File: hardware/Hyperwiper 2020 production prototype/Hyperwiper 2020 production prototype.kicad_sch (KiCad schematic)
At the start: 19 parts, among them K1 Main Power relay, K2 Wiper control relay, Q1 PN2222A, SW1 ON-OFF, U1 Teensy4.0, U3 L7805

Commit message: Updated Schematic and board.
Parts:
- added X1, X2: W237-3E-bGeigieNanoKit_V1.1r5a-eagle-import, DWP 2020:W237-3E, symbol import_from_eagle-rescue:W237-3E-bGeigieNanoKit_V1.1r5a-eagle-import
- RV1: footprint Potentiometer_THT:Potentiometer_Alps_RK09K_Single_Horizontal -> Potentiometer_THT:Potentiometer_Piher_PT-10-V05_Vertical
- U3: footprint Package_TO_SOT_THT:TO-220-3_Vertical -> Package_TO_SOT_THT:TO-220-3_Horizontal_TabUp
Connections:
- net GND: now also X1.1 (KL)
- net reed: now also X1.2 (KL)
- net at K1.1, K2.3: now also X2.1 (KL)
- net at K1.4, K1.5, K2.1: now also X2.2 (KL)
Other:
- moved on the sheet: S1
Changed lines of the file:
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@@
+    (stroke (width 0) (type solid) (color 0 0 0 0))
+  )
+  (wire (pts (xy 234.95 114.3) (xy 252.73 114.3))
+    (stroke (width 0) (type solid) (color 0 0 0 0))
+  )
+  (wire (pts (xy 234.95 116.84) (xy 242.57 116.84))
+    (stroke (width 0) (type solid) (color 0 0 0 0))
+  )
+  (wire (pts (xy 234.95 118.11) (xy 234.95 116.84))
     (stroke (width 0) (type solid) (color 0 0 0 0))
   )
@@
     (stroke (width 0) (type solid) (color 0 0 0 0))
   )
+  (wire (pts (xy 242.57 116.84) (xy 242.57 118.11))
+    (stroke (width 0) (type solid) (color 0 0 0 0))
+  )
+  (wire (pts (xy 242.57 127) (xy 242.57 134.62))
+    (stroke (width 0) (type solid) (color 0 0 0 0))
+  )
   (wire (pts (xy 245.11 52.07) (xy 252.73 52.07))
     (stroke (width 0) (type solid) (color 0 0 0 0))
@@
     (stroke (width 0) (type solid) (color 0 0 0 0))
   )
-  (wire (pts (xy 252.73 114.3) (xy 260.35 114.3))
+  (wire (pts (xy 252.73 114.3) (xy 252.73 118.11))
+    (stroke (width 0) (type solid) (color 0 0 0 0))
+  )
+  (wire (pts (xy 252.73 127) (xy 252.73 132.08))
+    (stroke (width 0) (type solid) (color 0 0 0 0))
+  )
+  (wire (pts (xy 252.73 144.78) (xy 252.73 149.86))
     (stroke (width 0) (type solid) (color 0 0 0 0))
   )
@@
     (stroke (width 0) (type solid) (color 0 0 0 0))
   )
-  (wire (pts (xy 260.35 123.19) (xy 260.35 114.3))
-    (stroke (width 0) (type solid) (color 0 0 0 0))
-  )
-  (wire (pts (xy 260.35 127) (xy 260.35 132.08))
-    (stroke (width 0) (type solid) (color 0 0 0 0))
-  )
-  (wire (pts (xy 260.35 144.78) (xy 260.35 149.86))
-    (stroke (width 0) (type solid) (color 0 0 0 0))
-  )
-  (wire (pts (xy 269.24 107.95) (xy 269.24 123.19))
+  (wire (pts (xy 269.24 107.95) (xy 269.24 118.11))
     (stroke (width 0) (type solid) (color 0 0 0 0))
   )
@@
     (stroke (width 0) (type solid) (color 0 0 0 0))
   )
-  (wire (pts (xy 275.59 105.41) (xy 275.59 123.19))
+  (wire (pts (xy 275.59 105.41) (xy 275.59 118.11))
     (stroke (width 0) (type solid) (color 0 0 0 0))
   )
@@
     (effects (font (size 1.27 1.27)) (justify right bottom))
   )
+  (label "reed" (at 234.95 114.3 180)
+    (effects (font (size 1.27 1.27)) (justify right bottom))
+  )
+  (label "car_gnd" (at 242.57 134.62 270)
+    (effects (font (size 1.27 1.27)) (justify right bottom))
+  )
   (label "5V" (at 248.92 20.32 180)
     (effects (font (size 1.27 1.27)) (justify right bottom))
   )
-  (label "reed" (at 252.73 114.3 180)
-    (effects (font (size 1.27 1.27)) (justify right bottom))
-  )
   (symbol (lib_id "power:GND") (at 118.11 86.36 0) (unit 1)
     (in_bom yes) (on_board yes)
-    (property "Reference" "#PWR?" (id 0) (at 118.11 92.71 0)
+    (property "Reference" "#PWR0109" (id 0) (at 118.11 92.71 0)
       (effects (font (size 1.27 1.27)) hide)
     )
@@
     )
   )
+  (symbol (lib_id "power:GND") (at 234.95 118.11 0) (unit 1)
+    (in_bom yes) (on_board yes)
+    (property "Reference" "#PWR0110" (id 0) (at 234.95 124.46 0)
+      (effects (font (size 1.27 1.27)) hide)
+    )
+    (property "Value" "GND" (id 1) (at 236.22 123.19 0))
+    (property "Footprint" "" (id 2) (at 234.95 118.11 0)
+      (effects (font (size 1.27 1.27)) hide)
+    )
+    (property "Datasheet" "" (id 3) (at 234.95 118.11 0)
+      (effects (font (size 1.27 1.27)) hide)
+    )
+  )
   (symbol (lib_id "power:GND") (at 241.3 40.64 0) (unit 1)
     (in_bom yes) (on_board yes)
@@
     )
   )
-  (symbol (lib_id "power:GND") (at 260.35 149.86 0) (unit 1)
-    (in_bom yes) (on_board yes)
-    (property "Reference" "#PWR0104" (id 0) (at 260.35 156.21 0)
-      (effects (font (size 1.27 1.27)) hide)
-    )
-    (property "Value" "GND" (id 1) (at 261.62 154.94 0))
-    (property "Footprint" "" (id 2) (at 260.35 149.86 0)
-      (effects (font (size 1.27 1.27)) hide)
-    )
-    (property "Datasheet" "" (id 3) (at 260.35 149.86 0)
+  (symbol (lib_id "power:GND") (at 252.73 149.86 0) (unit 1)
+    (in_bom yes) (on_board yes)
+    (property "Reference" "#PWR0104" (id 0) (at 252.73 156.21 0)
+      (effects (font (size 1.27 1.27)) hide)
+    )
+    (property "Value" "GND" (id 1) (at 254 154.94 0))
+    (property "Footprint" "" (id 2) (at 252.73 149.86 0)
+      (effects (font (size 1.27 1.27)) hide)
+    )
+    (property "Datasheet" "" (id 3) (at 252.73 149.86 0)
+      (effects (font (size 1.27 1.27)) hide)
+    )
+  )
+  (symbol (lib_id "import_from_eagle-rescue:W237-3E-bGeigieNanoKit_V1.1r5a-eagle-import") (at 242.57 123.19 90) (unit 1)
+    (in_bom yes) (on_board yes)
+    (property "Reference" "X1" (id 0) (at 245.11 119.38 0)
+      (effects (font (size 1.4986 1.4986)) (justify right))
+    )
+    (property "Value" "W237-3E-bGeigieNanoKit_V1.1r5a-eagle-import" (id 1) (at 245.11 121.92 90)
+      (effects (font (size 1.499 1.499)) (justify right) hide)
+    )
+    (property "Footprint" "DWP 2020:W237-3E" (id 2) (at 242.57 123.19 0)
+      (effects (font (size 1.27 1.27)) hide)
+    )
+    (property "Datasheet" "" (id 3) (at 242.57 123.19 0)
+      (effects (font (size 1.27 1.27)) hide)
+    )
+  )
+  (symbol (lib_id "import_from_eagle-rescue:W237-3E-bGeigieNanoKit_V1.1r5a-eagle-import") (at 252.73 123.19 90) (unit 2)
+    (in_bom yes) (on_board yes)
+    (property "Reference" "X1" (id 0) (at 255.27 119.38 0)
+      (effects (font (size 1.4986 1.4986)) (justify right))
+    )
+    (property "Value" "W237-3E-bGeigieNanoKit_V1.1r5a-eagle-import" (id 1) (at 255.27 121.92 90)
+      (effects (font (size 1.499 1.499)) (justify right) hide)
+    )
+    (property "Footprint" "DWP 2020:W237-3E" (id 2) (at 252.73 123.19 0)
+      (effects (font (size 1.27 1.27)) hide)
+    )
+    (property "Datasheet" "" (id 3) (at 252.73 123.19 0)
+      (effects (font (size 1.27 1.27)) hide)
+    )
+  )
+  (symbol (lib_id "import_from_eagle-rescue:W237-3E-bGeigieNanoKit_V1.1r5a-eagle-import") (at 269.24 123.19 90) (unit 1)
+    (in_bom yes) (on_board yes)
+    (property "Reference" "X2" (id 0) (at 271.78 119.38 0)
+      (effects (font (size 1.4986 1.4986)) (justify right))
+    )
+    (property "Value" "W237-3E-bGeigieNanoKit_V1.1r5a-eagle-import" (id 1) (at 271.78 121.92 90)
+      (effects (font (size 1.499 1.499)) (justify right) hide)
+    )
+    (property "Footprint" "DWP 2020:W237-3E" (id 2) (at 269.24 123.19 0)
+      (effects (font (size 1.27 1.27)) hide)
+    )
+    (property "Datasheet" "" (id 3) (at 269.24 123.19 0)
+      (effects (font (size 1.27 1.27)) hide)
+    )
+  )
+  (symbol (lib_id "import_from_eagle-rescue:W237-3E-bGeigieNanoKit_V1.1r5a-eagle-import") (at 275.59 123.19 90) (unit 2)
+    (in_bom yes) (on_board yes)
+    (property "Reference" "X2" (id 0) (at 278.13 119.38 0)
+      (effects (font (size 1.4986 1.4986)) (justify right))
+    )
+    (property "Value" "W237-3E-bGeigieNanoKit_V1.1r5a-eagle-import" (id 1) (at 278.13 121.92 90)
+      (effects (font (size 1.499 1.499)) (justify right) hide)
+    )
+    (property "Footprint" "DWP 2020:W237-3E" (id 2) (at 275.59 123.19 0)
+      (effects (font (size 1.27 1.27)) hide)
+    )
+    (property "Datasheet" "" (id 3) (at 275.59 123.19 0)
       (effects (font (size 1.27 1.27)) hide)
     )
@@
       (effects (font (size 1.27 1.27)) (justify right))
     )
-    (property "Footprint" "Potentiometer_THT:Potentiometer_Alps_RK09K_Single_Horizontal" (id 2) (at 161.29 160.02 0)
+    (property "Footprint" "Potentiometer_THT:Potentiometer_Piher_PT-10-V05_Vertical" (id 2) (at 161.29 160.02 0)
       (effects (font (size 1.27 1.27)) hide)
     )
@@
     )
   )
-  (symbol (lib_id "import_from_eagle-rescue:REED-SWITCH-CT10-A2-bGeigieNanoKit_V1.1r5a-eagle-import") (at 260.35 139.7 0) (unit 1)
-    (in_bom yes) (on_board yes)
-    (property "Reference" "S1" (id 0) (at 262.89 135.89 0)
+  (symbol (lib_id "import_from_eagle-rescue:REED-SWITCH-CT10-A2-bGeigieNanoKit_V1.1r5a-eagle-import") (at 252.73 139.7 0) (unit 1)
+    (in_bom yes) (on_board yes)
+    (property "Reference" "S1" (id 0) (at 255.27 135.89 0)
       (effects (font (size 1.4986 1.4986)) (justify left))
     )
-    (property "Value" "REED-SWITCH-CT10-A2-bGeigieNanoKit_V1.1r5a-eagle-import" (id 1) (at 262.89 139.7 0)
+    (property "Value" "REED-SWITCH-CT10-A2-bGeigieNanoKit_V1.1r5a-eagle-import" (id 1) (at 255.27 139.7 0)
       (effects (font (size 1.499 1.499)) (justify left) hide)
     )
-    (property "Footprint" "" (id 2) (at 260.35 139.7 0)
-      (effects (font (size 1.27 1.27)) hide)
-    )
-    (property "Datasheet" "" (id 3) (at 260.35 139.7 0)
+    (property "Footprint" "" (id 2) (at 252.73 139.7 0)
+      (effects (font (size 1.27 1.27)) hide)
+    )
+    (property "Datasheet" "" (id 3) (at 252.73 139.7 0)
       (effects (font (size 1.27 1.27)) hide)
     )
@@
     (property "Reference" "U3" (id 0) (at 241.3 21.59 0))
     (property "Value" "L7805" (id 1) (at 241.3 24.13 0))
-    (property "Footprint" "Package_TO_SOT_THT:TO-220-3_Vertical" (id 2) (at 241.935 33.02 0)
+    (property "Footprint" "Package_TO_SOT_THT:TO-220-3_Horizontal_TabUp" (id 2) (at 241.935 33.02 0)
       (effects (font (size 1.27 1.27) italic) (justify left) hide)
     )
@@
     )
     (path "/9b49453a-7d8c-46f7-ac72-5b7ca2259e26"
-      (reference "#PWR?") (unit 1)
+      (reference "#PWR0109") (unit 1)
+    )
+    (path "/8e8791e7-f5c8-46ac-8494-bdb46b4d3074"
+      (reference "#PWR0110") (unit 1)
     )
     (path "/3e7c7f71-990b-4b23-8faa-21bc92ed5e62"
@@
       (reference "U3") (unit 1)
     )
-  )
+    (path "/a84228e8-43cd-4089-b680-2e81d592d20a"
+      (reference "X1") (unit 1)
+    )
+    (path "/20235294-3224-4d0b-9ea7-1bc2750028c9"
+      (reference "X1") (unit 2)
+    )
+    (path "/7b8a6e5c-ae62-44de-ab03-2dc22e81d347"
+      (reference "X2") (unit 1)
+    )
+    (path "/0c382f83-c9eb-437e-a290-b66c0c4bdbe8"
+      (reference "X2") (unit 2)
+    )
+  )

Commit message: updated kicad files with new traced board
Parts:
- U3: footprint Package_TO_SOT_THT:TO-220-3_Horizontal_TabUp -> Package_TO_SOT_THT:TO-220-3_Vertical
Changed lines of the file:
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@@
-(kicad_sch (version 20200714) (host eeschema "5.99.0-unknown-a61ea1f~89~ubuntu20.04.1")
+(kicad_sch (version 20200714) (host eeschema "5.99.0-unknown-27d319b2d~89~ubuntu20.04.1")
   (page 1 1)
   (paper "A4")
@@
     (date "2020-07-25")
   )
-  (junction (at 179.07 20.32) (diameter 0) (color 0 0 0 0))
-  (junction (at 228.6 46.99) (diameter 0) (color 0 0 0 0))
-  (junction (at 252.73 52.07) (diameter 0) (color 0 0 0 0))
-  (junction (at 255.27 107.95) (diameter 0) (color 0 0 0 0))
-  (junction (at 275.59 105.41) (diameter 0) (color 0 0 0 0))
+  (junction (at 179.07 20.32) (diameter 0.2591) (color 0 0 0 0))
+  (junction (at 228.6 46.99) (diameter 0.2591) (color 0 0 0 0))
+  (junction (at 252.73 52.07) (diameter 0.2591) (color 0 0 0 0))
+  (junction (at 255.27 107.95) (diameter 0.2591) (color 0 0 0 0))
+  (junction (at 275.59 105.41) (diameter 0.2591) (color 0 0 0 0))
   (wire (pts (xy 107.95 83.82) (xy 140.97 83.82))
     (stroke (width 0) (type solid) (color 0 0 0 0))
@@
     (property "Reference" "U3" (id 0) (at 241.3 21.59 0))
     (property "Value" "L7805" (id 1) (at 241.3 24.13 0))
-    (property "Footprint" "Package_TO_SOT_THT:TO-220-3_Horizontal_TabUp" (id 2) (at 241.935 33.02 0)
+    (property "Footprint" "Package_TO_SOT_THT:TO-220-3_Vertical" (id 2) (at 241.935 33.02 0)
       (effects (font (size 1.27 1.27) italic) (justify left) hide)
     )

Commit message: Updated board
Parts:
- removed D1: Motor LED, LED_THT:LED_D5.0mm-4_RGB, symbol Device:LED_CRGB
- removed D2: Beat LED, LED_THT:LED_D5.0mm-4_RGB, symbol Device:LED_CRGB
- added D1: Motor LED, LED_THT:LED_D5.0mm-4_RGB, symbol Device:LED_RCBG
- added D2: Beat LED, LED_THT:LED_D5.0mm-4_RGB, symbol Device:LED_RCBG
- SW1: footprint (none) -> Button_Switch_THT:SW_Tactile_SPST_Angled_PTS645Vx83-2LFS
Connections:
- net GND: now also D1.2 (K), D2.2 (K)
- net at R6.2: now also D1.1 (RA)
- net at R5.2: now also D1.4 (GA)
- net at R4.2: now also D1.3 (BA)
- net at R7.2: now also D2.3 (BA)
- net at R8.2: now also D2.4 (GA)
- net at R9.2: now also D2.1 (RA)
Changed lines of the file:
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@@
-(kicad_sch (version 20200714) (host eeschema "5.99.0-unknown-27d319b2d~89~ubuntu20.04.1")
+(kicad_sch (version 20200714) (host eeschema "5.99.0-unknown-8c94d88c7~89~ubuntu20.04.1")
   (page 1 1)
   (paper "A4")
@@
     (property "Reference" "SW1" (id 0) (at 238.76 88.9 0))
     (property "Value" "ON-OFF" (id 1) (at 250.19 88.9 90))
-    (property "Footprint" "" (id 2) (at 245.11 88.9 0)
+    (property "Footprint" "Button_Switch_THT:SW_Tactile_SPST_Angled_PTS645Vx83-2LFS" (id 2) (at 245.11 88.9 0)
       (effects (font (size 1.27 1.27)) hide)
     )
@@
   (symbol (lib_id "Device:R_POT_TRIM") (at 161.29 160.02 180) (unit 1)
     (in_bom yes) (on_board yes)
-    (property "Reference" "RV1" (id 0) (at 163.83 158.75 0)
+    (property "Reference" "RV1" (id 0) (at 163.83 156.845 0)
       (effects (font (size 1.27 1.27)) (justify right))
     )
@@
   (symbol (lib_id "Transistor_BJT:PN2222A") (at 189.23 82.55 0) (unit 1)
     (in_bom yes) (on_board yes)
-    (property "Reference" "Q1" (id 0) (at 194.31 81.28 0)
+    (property "Reference" "Q1" (id 0) (at 194.4624 79.6544 0)
       (effects (font (size 1.27 1.27)) (justify left))
     )
@@
     )
   )
-  (symbol (lib_id "Device:LED_CRGB") (at 182.88 116.84 180) (unit 1)
-    (in_bom yes) (on_board yes)
-    (property "Reference" "D1" (id 0) (at 182.88 104.14 0))
-    (property "Value" "Motor LED" (id 1) (at 182.88 106.68 0))
+  (symbol (lib_id "Device:LED_RCBG") (at 182.88 116.84 180) (unit 1)
+    (in_bom yes) (on_board yes)
+    (property "Reference" "D1" (id 0) (at 187.96 109.855 0))
+    (property "Value" "Motor LED" (id 1) (at 183.515 126.365 0))
     (property "Footprint" "LED_THT:LED_D5.0mm-4_RGB" (id 2) (at 182.88 115.57 0)
       (effects (font (size 1.27 1.27)) hide)
@@
     )
   )
-  (symbol (lib_id "Device:LED_CRGB") (at 182.88 137.16 180) (unit 1)
-    (in_bom yes) (on_board yes)
-    (property "Reference" "D2" (id 0) (at 182.88 124.46 0))
-    (property "Value" "Beat LED" (id 1) (at 182.88 127 0))
+  (symbol (lib_id "Device:LED_RCBG") (at 182.88 137.16 180) (unit 1)
+    (in_bom yes) (on_board yes)
+    (property "Reference" "D2" (id 0) (at 187.96 130.81 0))
+    (property "Value" "Beat LED" (id 1) (at 183.515 147.32 0))
     (property "Footprint" "LED_THT:LED_D5.0mm-4_RGB" (id 2) (at 182.88 135.89 0)
       (effects (font (size 1.27 1.27)) hide)
@@
       (reference "#PWR0110") (unit 1)
     )
-    (path "/3e7c7f71-990b-4b23-8faa-21bc92ed5e62"
+    (path "/2723ac12-21fb-4eb0-b91d-4ea3a28c8ae0"
       (reference "D1") (unit 1)
     )
-    (path "/83ccb75b-41e2-4da1-b59a-2bb55bc93cc7"
+    (path "/a626228a-9c73-4fcc-9148-d4b02f6a1a48"
       (reference "D2") (unit 1)
     )

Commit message: Updated  schematic
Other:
- note added: "Pins: OUT: Motor on/off = Motor LED B = Motor LED G = Motor LED R = Beat B = Beat G = Beat R = IN: Reed-switch = PotentMeter ="
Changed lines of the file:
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@@
-(kicad_sch (version 20200714) (host eeschema "5.99.0-unknown-8c94d88c7~89~ubuntu20.04.1")
+(kicad_sch (version 20200714) (host eeschema "5.99.0-unknown-96f4e8f6f~89~ubuntu20.04.1")
   (page 1 1)
   (paper "A4")
   (title_block
     (title "Prototype board")
-    (date "2020-07-25")
+    (date "2020-08-19")
   )
   (junction (at 179.07 20.32) (diameter 0.2591) (color 0 0 0 0))
@@
     (stroke (width 0) (type solid) (color 0 0 0 0))
   )
+  (text "Pins:\n\nOUT:\nMotor on/off	=\nMotor LED B 	=\nMotor LED G 	=\nMotor LED R 	=\nBeat B 			=\nBeat G			=\nBeat R			=\n\nIN:\nReed-switch	=\nPotentMeter		=\n\n\n\n"
+    (at 53.975 149.86 0)
+    (effects (font (size 1.27 1.27)) (justify left bottom))
+  )
   (text "Notes:\n" (at 179.07 179.07 0)

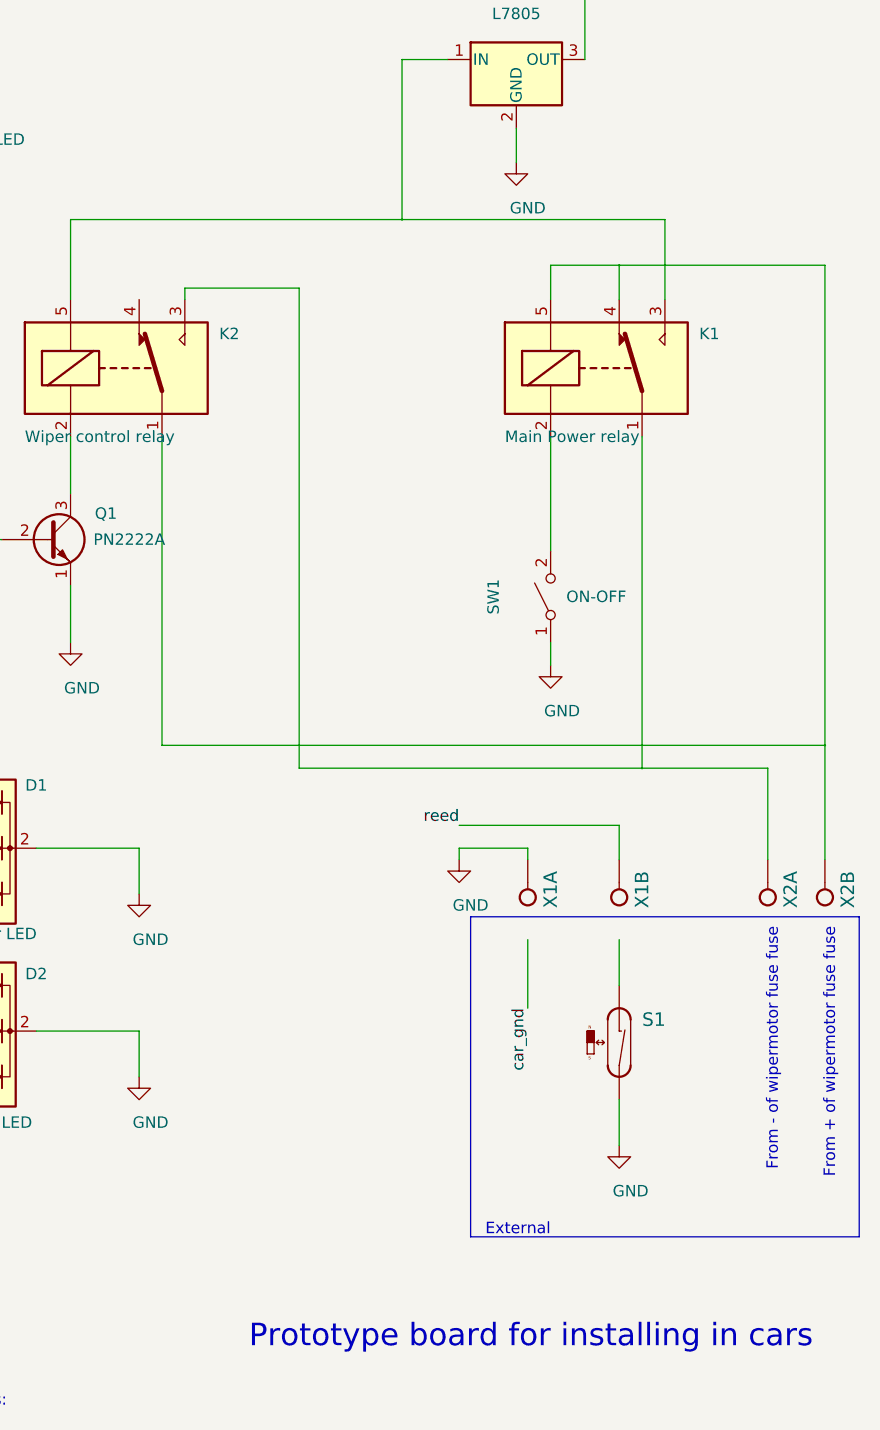
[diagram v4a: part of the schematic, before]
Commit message: Changes schemtic. Mistake in wireing
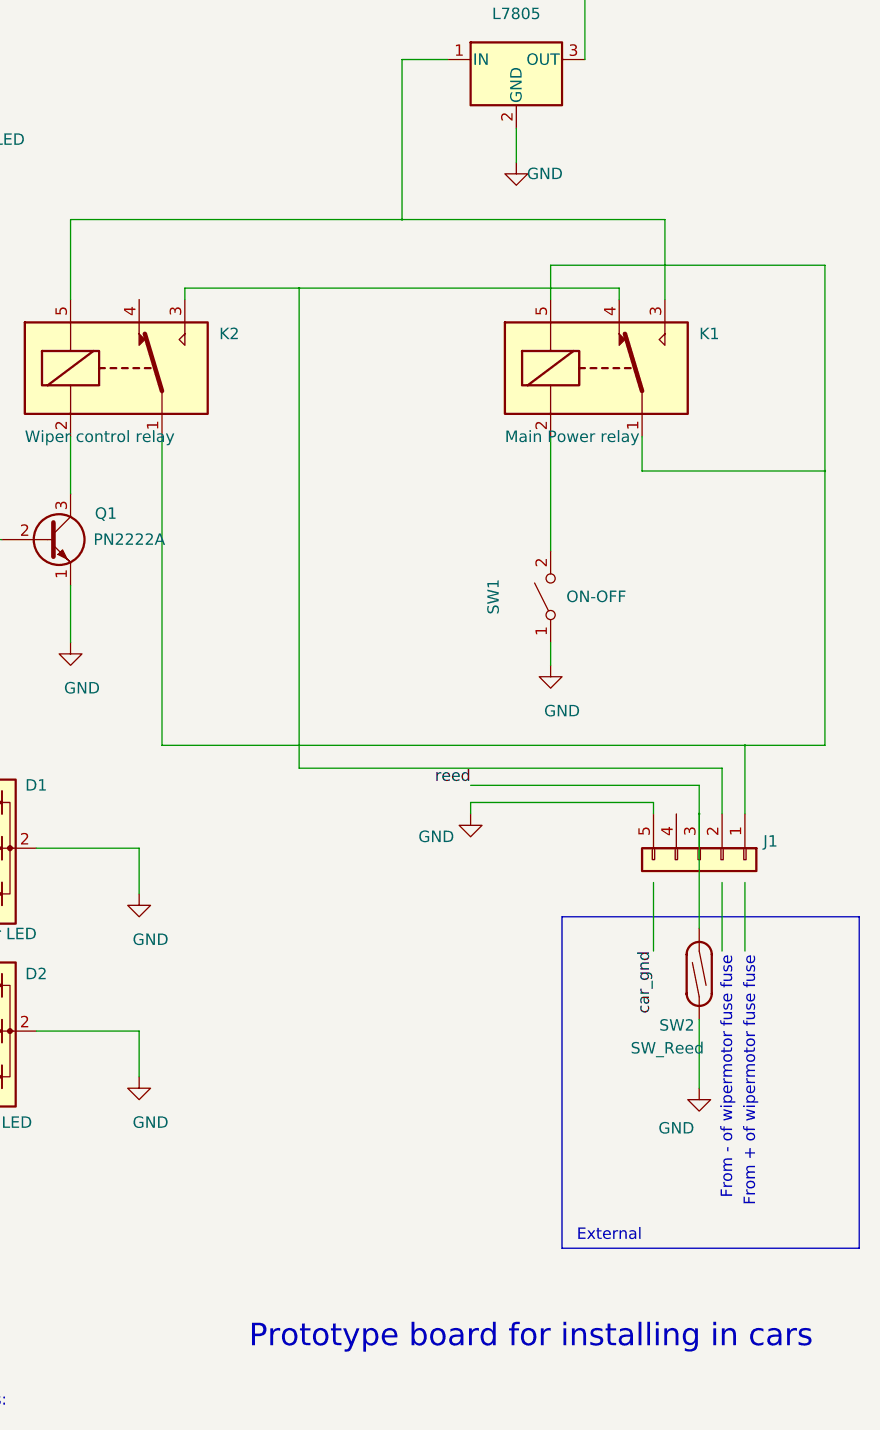
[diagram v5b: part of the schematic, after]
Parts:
- removed S1: REED-SWITCH-CT10-A2-bGeigieNanoKit_V1.1r5a-eagle-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, symbol import_from_eagle-rescue:REED-SWITCH-CT10-A2-bGeigieNanoKit_V1.1r5a-eagle-import
- removed X1, X2: W237-3E-bGeigieNanoKit_V1.1r5a-eagle-import, DWP 2020:W237-3E, symbol import_from_eagle-rescue:W237-3E-bGeigieNanoKit_V1.1r5a-eagle-import
- added J1: Conn_01x05, TerminalBlock_MetzConnect:TerminalBlock_MetzConnect_Type011_RT05505HBWC_1x05_P5.00mm_Horizontal, symbol Connector_Generic:Conn_01x05
- added SW2: SW_Reed, SW_SPST_REED_CT10-XXXX-G1, symbol Switch:SW_Reed
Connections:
- net GND: now also J1.5 (Pin_5), SW2.2
- net reed: now also J1.3 (Pin_3), SW2.1
- net at K1.5, K2.1: now also K1.1, J1.1 (Pin_1); no longer K1.4
- net at K2.3: now also K1.4, J1.2 (Pin_2); no longer K1.1
